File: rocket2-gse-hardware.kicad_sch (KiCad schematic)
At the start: 45 parts, among them J8 Conn_01x02_Pin, U15 LP2950, U16 AP2120N-3.3TRG1, Y1 16MHz

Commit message: fixed resistor values
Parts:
- added R49: 70k, Resistor_SMD:R_0402_1005Metric, symbol Device:R_Small_US
- added R50: 10k, Resistor_SMD:R_0402_1005Metric, symbol Device:R_Small_US
- J1: value ~ -> USB_C Connector; Manufacturer (none) -> Wurth Elektronik; Part # (none) -> 629105150521
- R13, R14: Manufacturer (none) -> Generic; Part # (none) -> Generic 5K1 0402 Resistor
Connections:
- net +24V: now also R49.1; no longer U1.26 (PB0)
- net GND: now also R50.2
- new net PWR: R49.2, R50.1, U1.26 (PB0)
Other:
- note added: "USBC"
- moved on the sheet: C9, J1, J8, R13, R14, U1, Y1

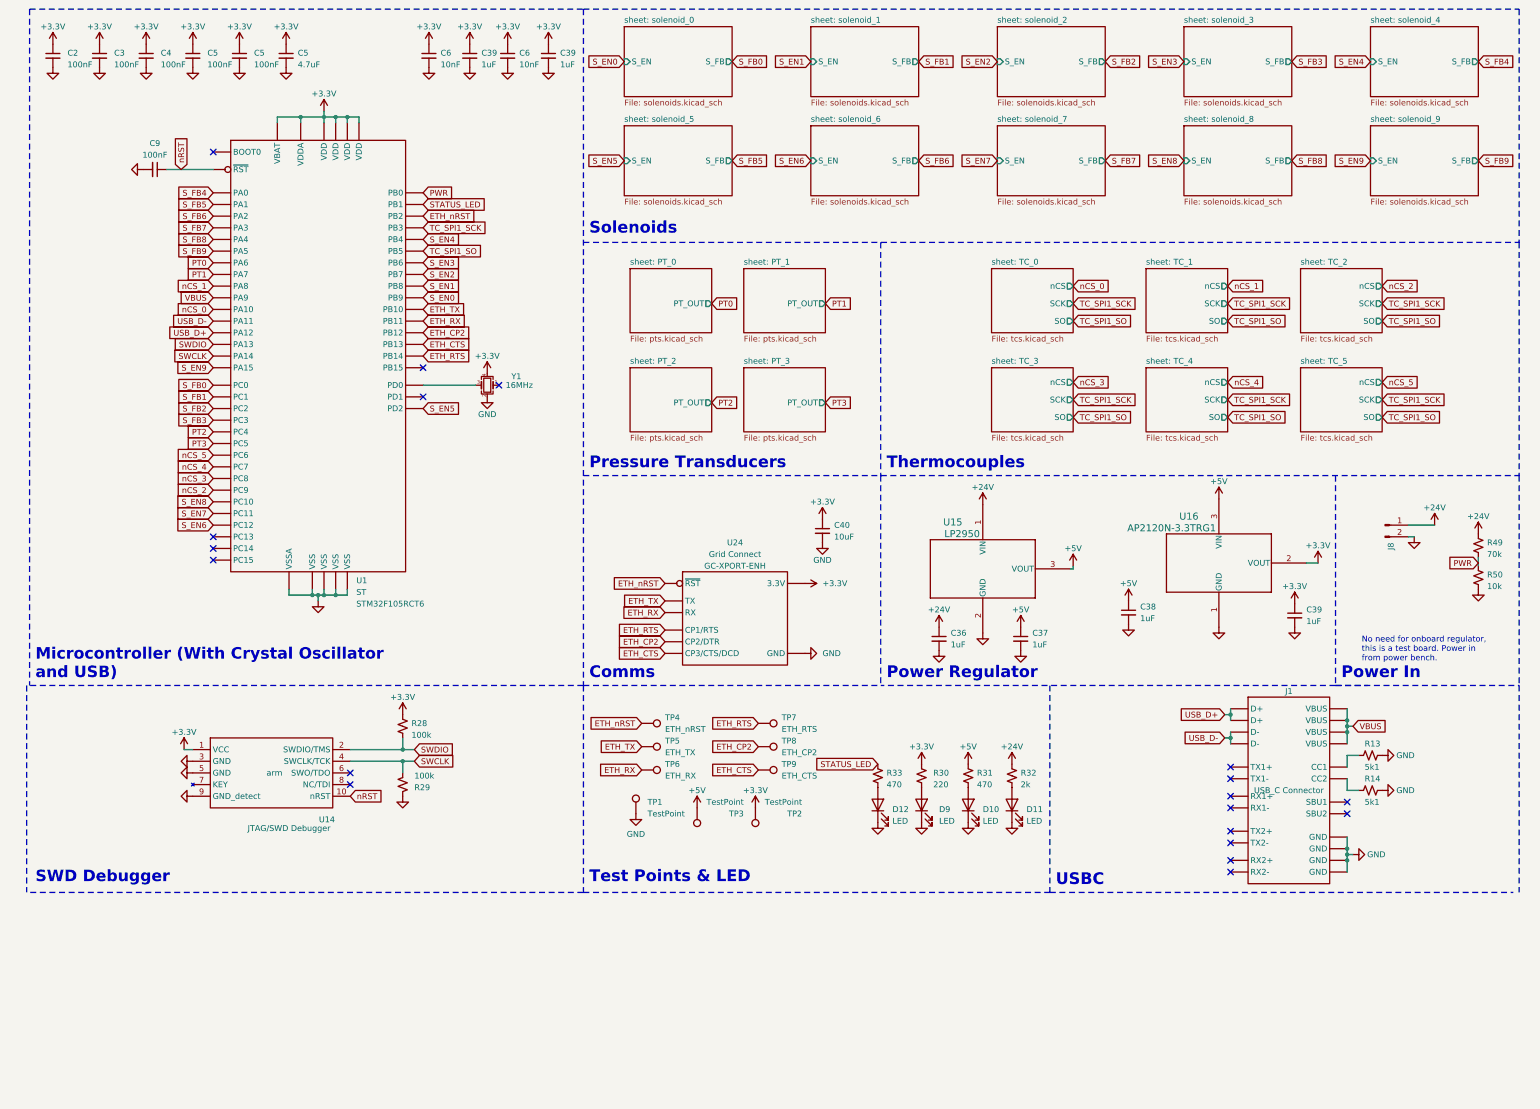
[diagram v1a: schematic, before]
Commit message: added full schematic and outdated pcb
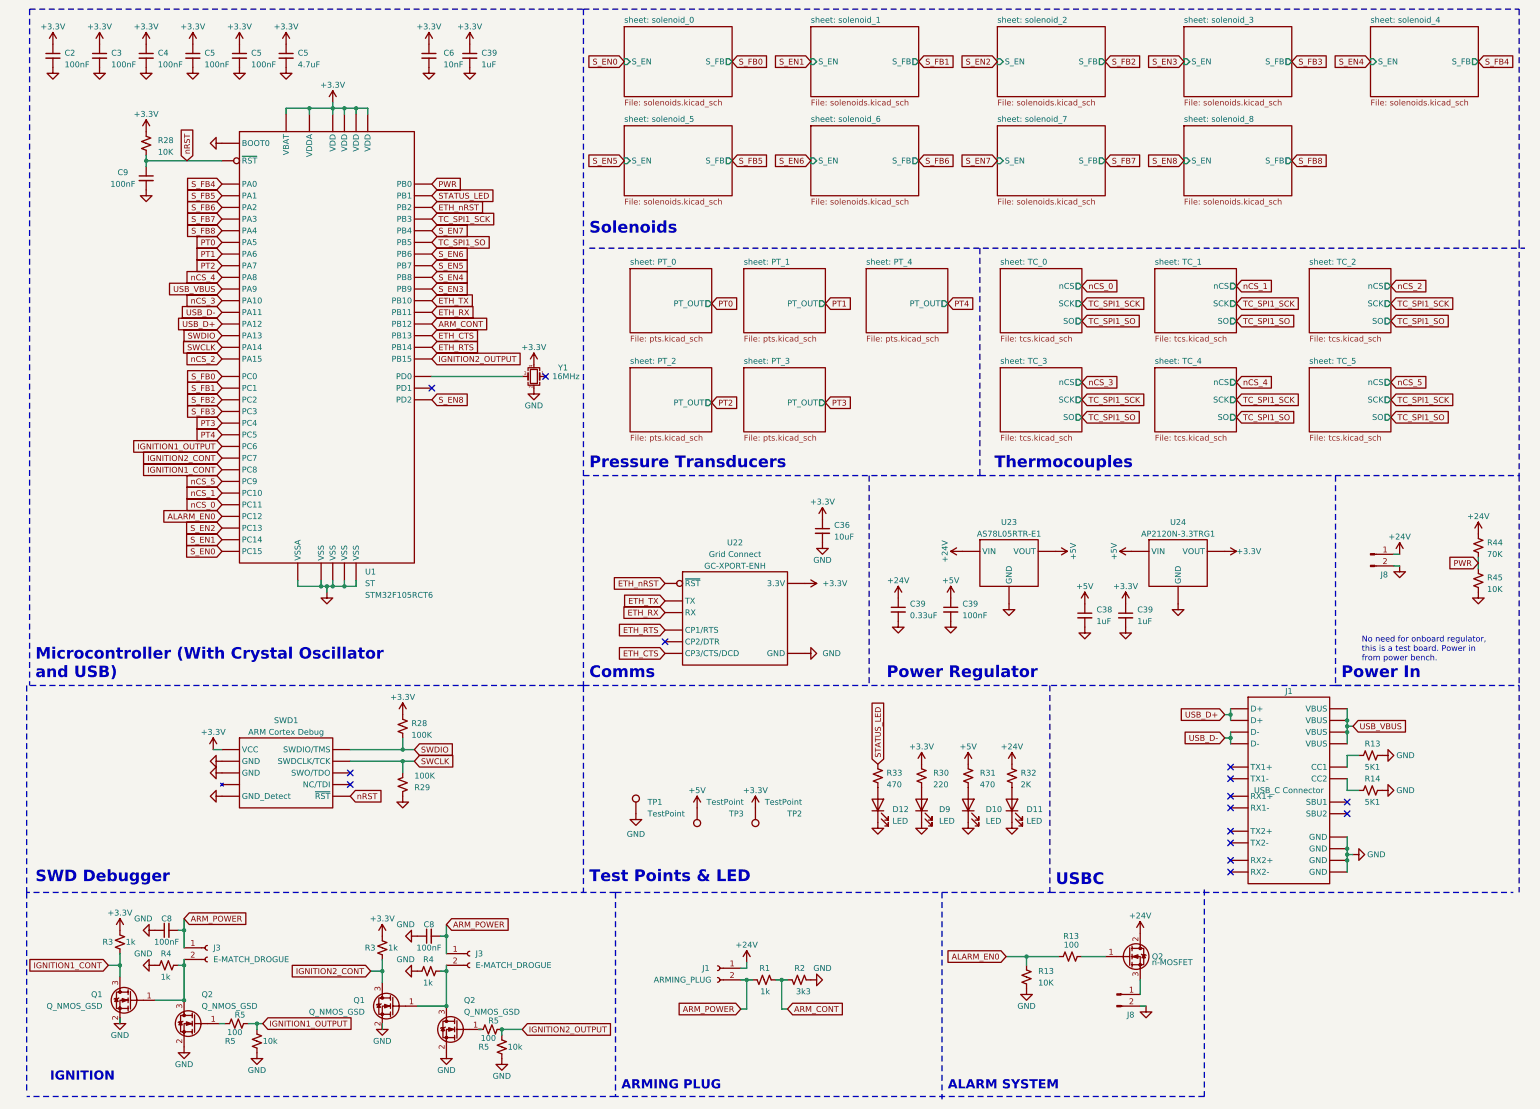
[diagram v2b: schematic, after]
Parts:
- removed C36: 1uF, Capacitor_SMD:C_0805_2012Metric, symbol Device:C_Small
- removed C37, C39: 1uF, Capacitor_SMD:C_0402_1005Metric, symbol Device:C_Small
- removed C6: 10nF, Capacitor_SMD:C_0402_1005Metric, symbol Device:C_Small
- removed TP4: ETH_nRST, TestPoint:TestPoint_Pad_D1.0mm, symbol Connector:TestPoint
- removed TP5: ETH_TX, TestPoint:TestPoint_Pad_D1.0mm, symbol Connector:TestPoint
- removed TP6: ETH_RX, TestPoint:TestPoint_Pad_D1.0mm, symbol Connector:TestPoint
- removed TP7: ETH_RTS, TestPoint:TestPoint_Pad_D1.0mm, symbol Connector:TestPoint
- removed TP8: ETH_CP2, TestPoint:TestPoint_Pad_D1.0mm, symbol Connector:TestPoint
- removed TP9: ETH_CTS, TestPoint:TestPoint_Pad_D1.0mm, symbol Connector:TestPoint
- removed U14: ~, Connector_PinHeader_1.27mm:PinHeader_2x05_P1.27mm_Vertical_SMD, symbol UCIRP-Symbols:JTAG/SWD_Connector
- removed U15: LP2950, Package_TO_SOT_SMD:TO-252-2, symbol 2023-12-08_09-46-53:AP2120N-3.3TRG1
- removed U16: AP2120N-3.3TRG1, Package_TO_SOT_SMD:SOT-23-3, symbol 2023-12-08_09-46-53:AP2120N-3.3TRG1
- added C39: 100nF, Capacitor_SMD:C_0402_1005Metric, symbol UCIRP-KiCAD-Lib:C_Small
- added C39: 0.33uF, Capacitor_SMD:C_0402_1005Metric, symbol UCIRP-KiCAD-Lib:C_Small
- added C8 (x2): 100nF, Capacitor_SMD:C_0603_1608Metric, symbol Device:C_Small
- added J1: ARMING_PLUG, TerminalBlock:TerminalBlock_bornier-2_P5.08mm, symbol Connector:Conn_01x02_Socket
- added J3 (x2): E-MATCH_DROGUE, TerminalBlock:TerminalBlock_bornier-2_P5.08mm, symbol Connector:Conn_01x02_Socket
- added J8: Conn_01x02_Pin, TerminalBlock:TerminalBlock_bornier-2_P5.08mm, symbol UCIRP-KiCAD-Lib:Conn_01x02_Pin
- added Q1 (x2), Q2 (x2): Q_NMOS_GSD, Package_TO_SOT_SMD:TSOT-23, symbol Device:Q_NMOS_GSD
- added Q2: n-MOSFET, Package_TO_SOT_SMD:SOT-23-3, symbol UCIRP-KiCAD-Lib:Q_NMOS_GDS
- added R1, R3 (x2), R4 (x2): 1k, Resistor_SMD:R_0603_1608Metric, symbol Device:R_Small_US
- added R13, R28: 10K, Resistor_SMD:R_0402_1005Metric, symbol UCIRP-KiCAD-Lib:R_Small_US
- added R13: 100, Resistor_SMD:R_0402_1005Metric, symbol UCIRP-KiCAD-Lib:R_Small_US
- added R2: 3k3, Resistor_SMD:R_0603_1608Metric, symbol Device:R_Small_US
- added R5 (x2): 100, Resistor_SMD:R_0603_1608Metric, symbol Device:R_Small_US
- added R5 (x2): 10k, Resistor_SMD:R_0603_1608Metric, symbol Device:R_Small_US
- added SWD1: ARM Cortex Debug, Connector_PinHeader_1.27mm:PinHeader_2x05_P1.27mm_Vertical_SMD, symbol UCIRP-KiCAD-Lib:ARM_Cortex_Debug
- added U23: ~, Package_TO_SOT_SMD:SOT-89-3, symbol UCIRP-KiCAD-Lib:Generic_Regulator_OutputGroundInput
- added U24: ~, Package_TO_SOT_SMD:SOT-23-3, symbol UCIRP-KiCAD-Lib:Generic_Regulator_GroundOutputInput
- C2, C3, C38, C39, C4, C5, C6, C9: symbol Device:C_Small -> UCIRP-KiCAD-Lib:C_Small
- C36: renamed from C40; footprint Capacitor_SMD:C_0603_1608Metric -> Capacitor_SMD:C_0402_1005Metric; symbol Device:C_Small -> UCIRP-KiCAD-Lib:C_Small; Part # Generic 0603 10uF 6.3V X7R MLCC -> Generic 10uF 0402 Capacitor
- C5: symbol Device:C_Small -> UCIRP-KiCAD-Lib:C_Small; Part # Generic 100nF 0402 Capacitor -> Generic 4.7uF 0402 Capacitor
- D10: symbol Device:LED -> UCIRP-KiCAD-Lib:LED; Part # Generic 0603 Yellow LED -> Generic 0603 Red LED
- D11, D12: symbol Device:LED -> UCIRP-KiCAD-Lib:LED
- D9: symbol Device:LED -> UCIRP-KiCAD-Lib:LED; Part # Generic 0603 Green LED -> Generic 0603 Red LED
- J8: symbol Connector:Conn_01x02_Pin -> UCIRP-KiCAD-Lib:Conn_01x02_Pin
- R13, R14: value 5k1 -> 5K1; footprint Resistor_SMD:R_0603_1608Metric -> Resistor_SMD:R_0402_1005Metric; symbol Device:R_Small_US -> UCIRP-KiCAD-Lib:R_Small_US
- R28, R29: value 100k -> 100K; symbol Device:R_Small_US -> UCIRP-KiCAD-Lib:R_Small_US
- R30, R31, R33: symbol Device:R_Small_US -> UCIRP-KiCAD-Lib:R_Small_US
- R32: value 2k -> 2K; symbol Device:R_Small_US -> UCIRP-KiCAD-Lib:R_Small_US
- R44: renamed from R49; value 70k -> 70K; symbol Device:R_Small_US -> UCIRP-KiCAD-Lib:R_Small_US
- R45: renamed from R50; value 10k -> 10K; symbol Device:R_Small_US -> UCIRP-KiCAD-Lib:R_Small_US
- TP1, TP2, TP3: symbol Connector:TestPoint -> UCIRP-KiCAD-Lib:TestPoint
- Y1: footprint Crystal:Crystal_SMD_2520-4Pin_2.5x2.0mm -> Crystal:Crystal_SMD_2016-4Pin_2.0x1.6mm; symbol Device:Crystal_GND24_Small -> UCIRP-KiCAD-Lib:Crystal_GND24_Small
- renumbered U24 to U22
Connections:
- net S_EN9 is gone; now on net nCS_2: U1.50 (PA15)
- net S_FB9 is gone; now on net PT0: U1.21 (PA5)
- net +24V: now also C39.1, J1.1 (Pin_1), Q2.2 (D), U23.3 (VIN)
- net +3.3V: now also R28.1, R3.1, R3.1, SWD1.1 (VCC), U24.2 (VOUT)
- net +5V: now also C39.1, U23.1 (VOUT), U24.3 (VIN)
- net GND: now also U1.60 (BOOT0), C39.2, C39.2, C8.1, C8.1, J8.2 (Pin_2), Q1.2 (S), Q1.2 (S), Q2.2 (S), Q2.2 (S), R13.2, R2.2, R4.2, R4.2, R5.2, R5.2, SWD1.3 (GND), SWD1.5 (GND), SWD1.9 (GND_Detect), U23.2 (GND), U24.1 (GND)
- net PT0: no longer U1.22 (PA6)
- net PT1: now also U1.22 (PA6); no longer U1.23 (PA7)
- net PT2: now also U1.23 (PA7); no longer U1.24 (PC4)
- net PT3: now also U1.24 (PC4); no longer U1.25 (PC5)
- net SWCLK: now also SWD1.4 (SWDCLK/TCK)
- net SWDIO: now also SWD1.2 (SWDIO/TMS)
- net S_EN0: now also U1.4 (PC15); no longer U1.62 (PB9)
- net S_EN1: now also U1.3 (PC14); no longer U1.61 (PB8)
- net S_EN2: now also U1.2 (PC13); no longer U1.59 (PB7)
- net S_EN3: now also U1.62 (PB9); no longer U1.58 (PB6)
- net S_EN4: now also U1.61 (PB8); no longer U1.56 (PB4)
- net S_EN5: now also U1.59 (PB7); no longer U1.54 (PD2)
- net S_EN6: now also U1.58 (PB6); no longer U1.53 (PC12)
- net S_EN7: now also U1.56 (PB4); no longer U1.52 (PC11)
- net S_EN8: now also U1.54 (PD2); no longer U1.51 (PC10)
- net nCS_0: now also U1.52 (PC11); no longer U1.43 (PA10)
- net nCS_1: now also U1.51 (PC10); no longer U1.41 (PA8)
- net nCS_2: no longer U1.40 (PC9)
- net nCS_3: now also U1.43 (PA10); no longer U1.39 (PC8)
- net nCS_4: now also U1.41 (PA8); no longer U1.38 (PC7)
- net nCS_5: now also U1.40 (PC9); no longer U1.37 (PC6)
- net nRST: now also R28.2, SWD1.10 (~{RST})
- net IGNITION2_OUTPUT: now reaches U1.36 (PB15)
- net IGNITION2_OUTPUT: now also R5.1, R5.2
- net ETH_CP2: no longer names the net of U22.7 (CP2/DTR)
- net ETH_CP2: no longer U1.33 (PB12)
- net VBUS renamed USB_VBUS
- new net: Q2.1 (G), R5.1 (x2)
- new net: J3.2 (Pin_2), Q1.1 (G), Q2.3 (D), R4.1 (x2)
- new net: Q2.1 (G), R13.2
- new net: J8.1 (Pin_1), Q2.3 (S)
- new net ALARM_EN0: R13.1, R13.1, U1.53 (PC12)
- new net ARM_CONT: R1.2, R2.1, U1.33 (PB12)
- new net ARM_POWER: C8.2, C8.2, J1.2 (Pin_2), J3.1 (Pin_1), J3.1 (Pin_1), R1.1
- new net IGNITION1_CONT: Q1.3 (D), R3.2, U1.39 (PC8)
- new net IGNITION1_OUTPUT: R5.1, R5.2, U1.37 (PC6)
- new net IGNITION2_CONT: Q1.3 (D), R3.2, U1.38 (PC7)
- new net PT4: U1.25 (PC5)
- no-connect marks 19 -> 15
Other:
- removed sheet sheet: solenoid_9
- added sheet sheet: PT_4 (pts.kicad_sch)
- note added: "ALARM SYSTEM"
- note added: "ARMING PLUG"
- note added: "IGNITION"
- moved on the sheet: C38, C39, C9, J8, R45, U1, Y1

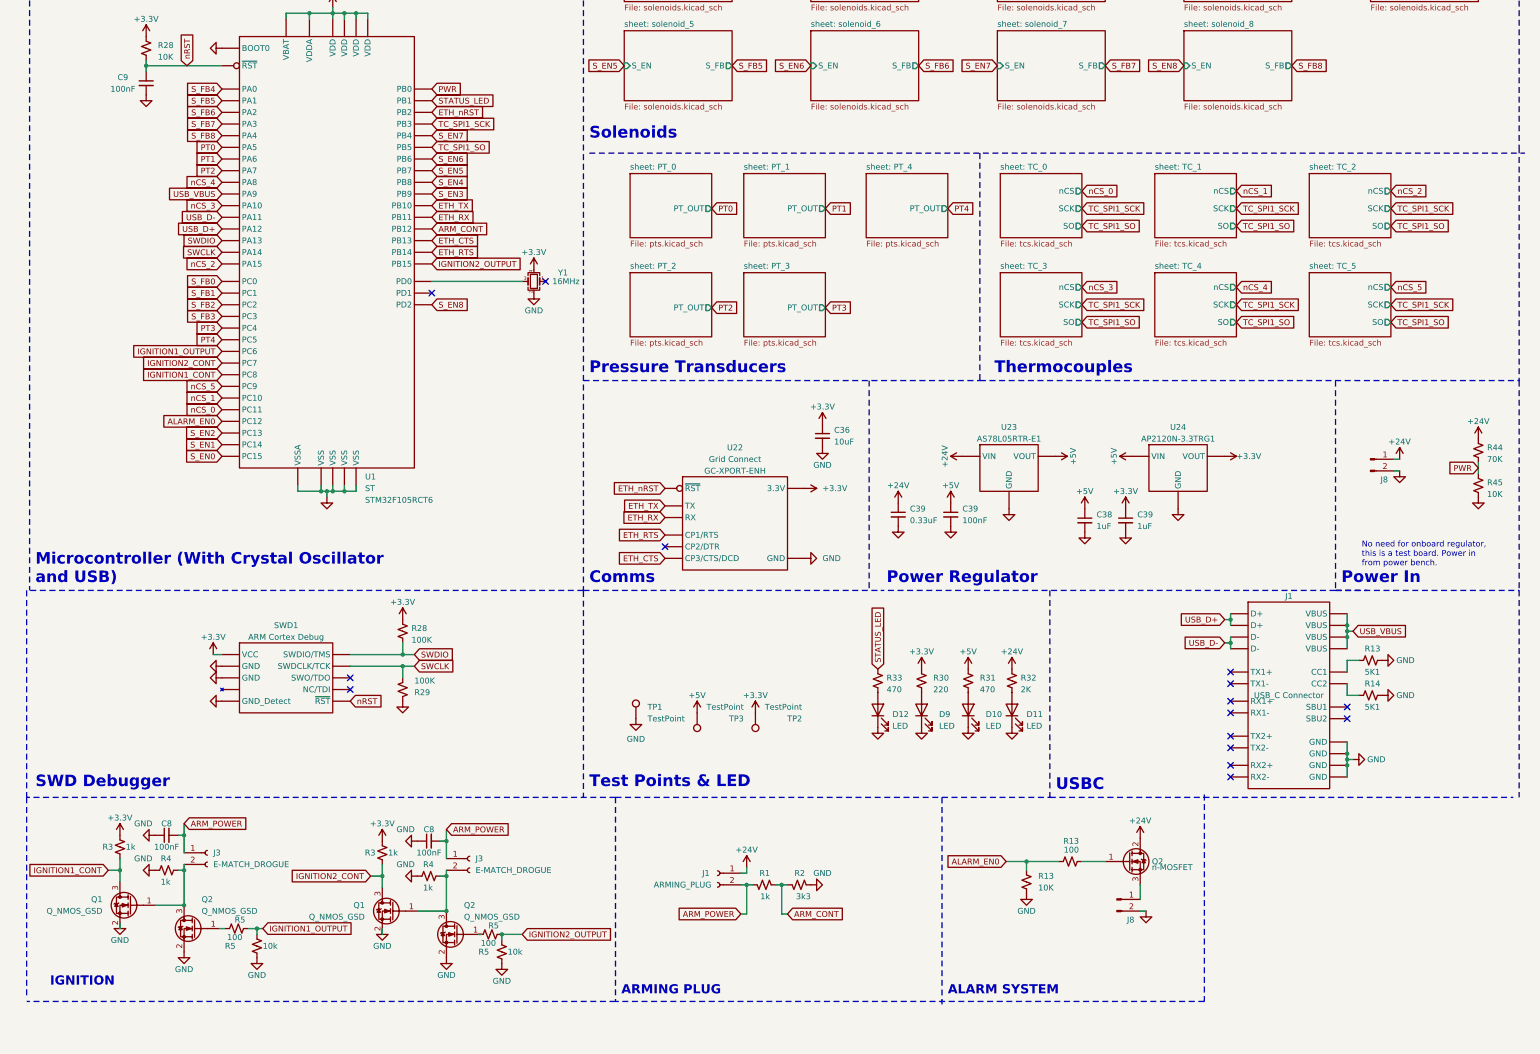
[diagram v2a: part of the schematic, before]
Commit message: final polished schematic b4 daniel fixes nmosfet and ignition circuit
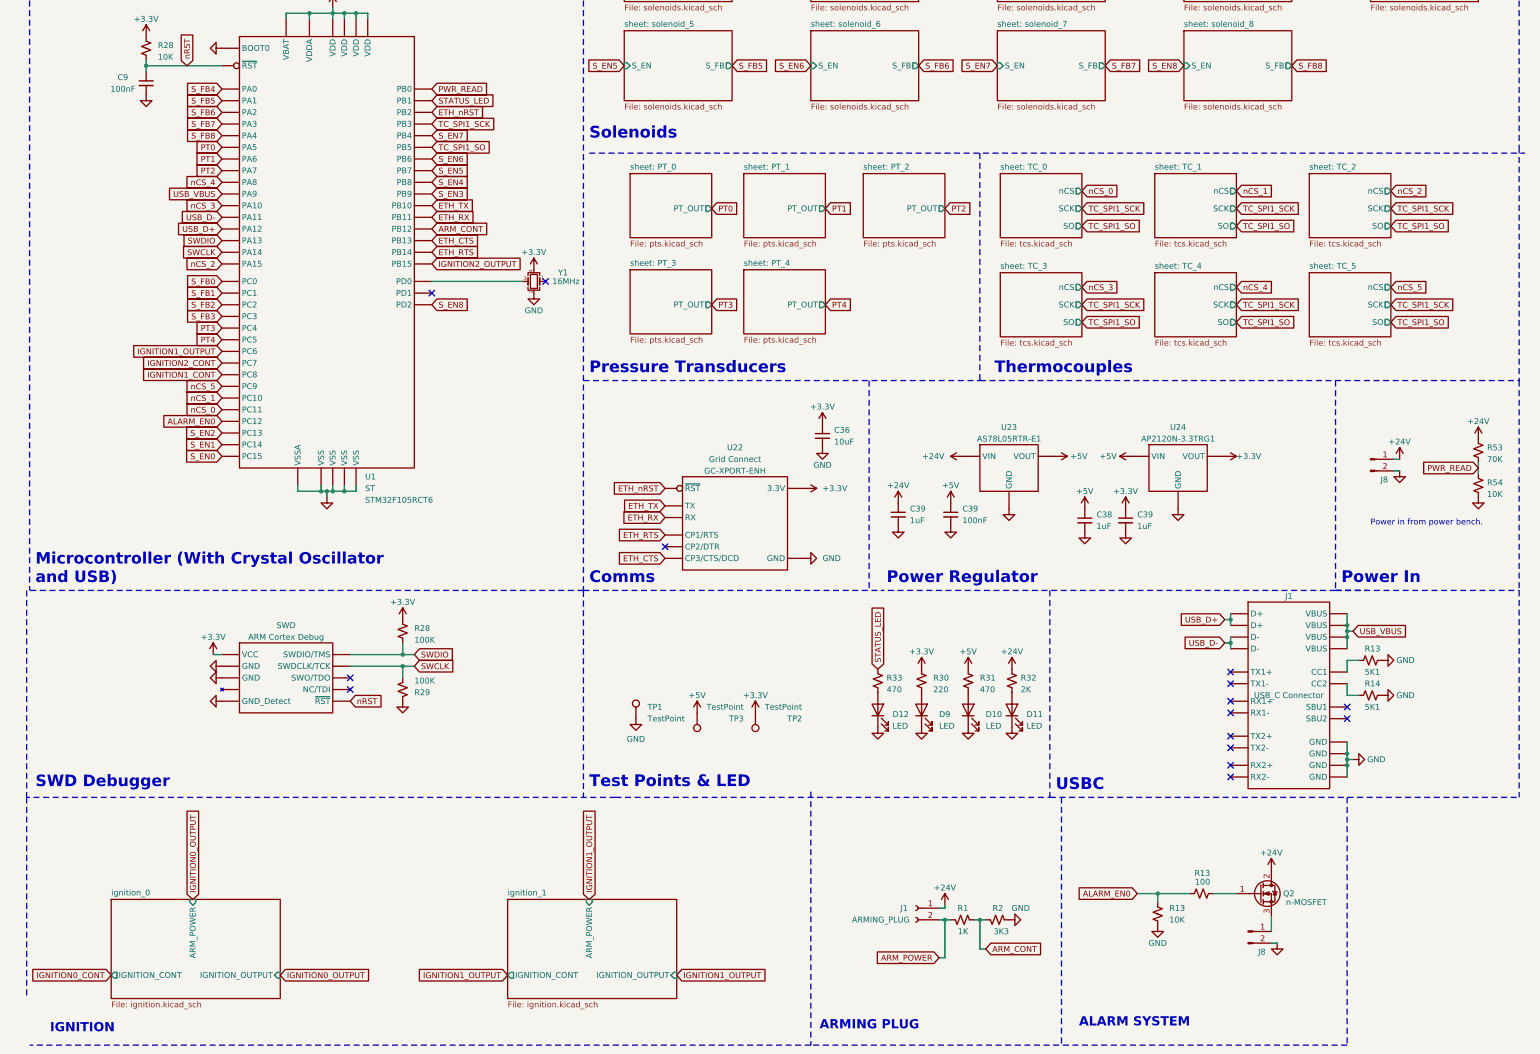
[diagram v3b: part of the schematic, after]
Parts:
- removed C8 (x2): 100nF, Capacitor_SMD:C_0603_1608Metric, symbol Device:C_Small
- removed J3 (x2): E-MATCH_DROGUE, TerminalBlock:TerminalBlock_bornier-2_P5.08mm, symbol Connector:Conn_01x02_Socket
- removed Q1 (x2), Q2 (x2): Q_NMOS_GSD, Package_TO_SOT_SMD:TSOT-23, symbol Device:Q_NMOS_GSD
- removed R3 (x2), R4 (x2): 1k, Resistor_SMD:R_0603_1608Metric, symbol Device:R_Small_US
- removed R5 (x2): 100, Resistor_SMD:R_0603_1608Metric, symbol Device:R_Small_US
- removed R5 (x2): 10k, Resistor_SMD:R_0603_1608Metric, symbol Device:R_Small_US
- C39: value 0.33uF -> 1uF; Part # Generic 0.33uF 0402 Capacitor -> Generic 1uF 0402 Capacitor
- J1: Manufacturer (none) -> Generic; Part # (none) -> Generic 2x5.08 Screw Terminal
- R1: value 1k -> 1K; footprint Resistor_SMD:R_0603_1608Metric -> Resistor_SMD:R_0402_1005Metric; Manufacturer (none) -> Generic; Part # (none) -> Generic 1K 0402 Resistor
- R13: Part # Generic 10K 0402 Resistor -> Generic 100 0402 Resistor
- R2: value 3k3 -> 3K3; footprint Resistor_SMD:R_0603_1608Metric -> Resistor_SMD:R_0402_1005Metric; Manufacturer (none) -> Generic; Part # (none) -> Generic 3K3 0402 Resistor
- renumbered R44 to R53, R45 to R54, SWD1 to SWD
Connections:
- net PWR renamed PWR_READ
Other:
- added sheet ignition_0 (ignition.kicad_sch)
- added sheet ignition_1 (ignition.kicad_sch)
- note added: "Power in from power bench."
- note removed: "No need for onboard regulator, this is a test board. Power in from power bench."
- moved on the sheet: J1, J8, Q2, R1, R13, R2
